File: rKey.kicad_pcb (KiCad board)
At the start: 2 copper layers, 52.8 x 71.4 mm, 39 parts, among them IC1 BDX34C, J1 Conn_01x06, Q1 BC337, Q2 BC337, Q3 BC337, Q4 BC337, Q5 BC327, Q8 BC337, U1 TL084BCN, U2 LM7810_TO220

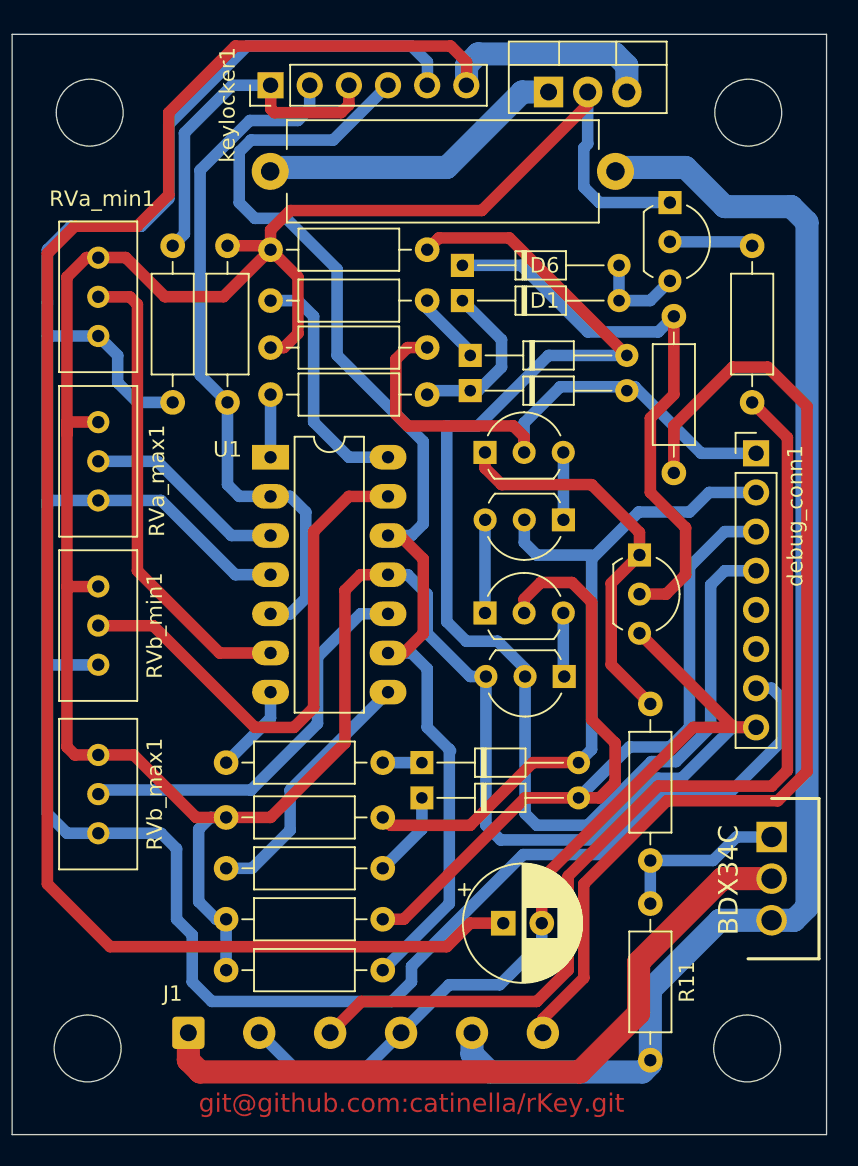
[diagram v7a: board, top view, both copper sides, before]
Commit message: Fix: unuseful (diodes) components removed
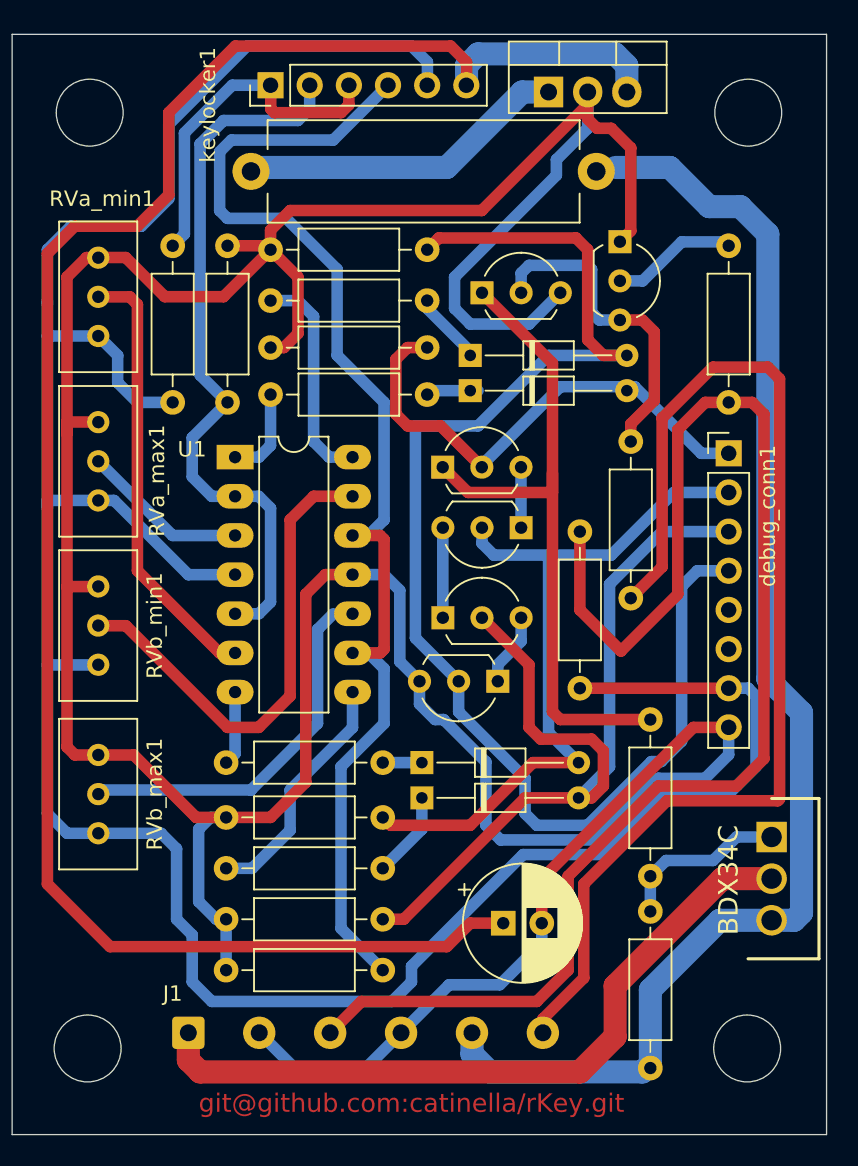
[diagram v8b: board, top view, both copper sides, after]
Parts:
- removed D1, D6: DIODE, Diode_THT:D_DO-34_SOD68_P10.16mm_Horizontal
- added R14: 100K, Resistor_THT:R_Axial_DIN0207_L6.3mm_D2.5mm_P10.16mm_Horizontal, F.Cu at (153.4, 99.1)
- moved Q8 19.8 mm to (147.1, 73.4), turned to 0 degrees
- moved R9 8.59 mm to (156.7, 83.1)
- moved Q4 4.32 mm to (148.1, 98.6)
- moved Q5 4.12 mm to (156.0, 70.1)
- moved Q1 2.91 mm to (144.5, 84.7)
- moved Q2 2.79 mm to (149.6, 88.6)
- moved Q3 2.75 mm to (144.5, 94.5)
- moved U1 2.30 mm to (131.0, 84.1)
- moved debug_conn1 1.78 mm to (163.1, 83.8)
- moved R13 1.52 mm to (163.1, 70.4)
- moved R6 1.25 mm to (132.1, 65.5)
- moved R10 1.02 mm to (158.0, 101.1)
- moved R11 0.51 mm to (158.0, 113.5)
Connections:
- Q5 pad 3: Net-(D1-Pad2) -> Net-(Q8-Pad2)
- Q8 pad 2: Net-(D6-Pad1) -> Net-(Q8-Pad2)
- R9 pad 1: Net-(D6-Pad1) -> Net-(Q8-Pad2)
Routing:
- net Net-(D6-Pad1): track 37.8 -> 0.00 mm
- net Net-(R14-Pad2): track 65.1 -> 92.8 mm
- net Net-(Q8-Pad2): track 0.00 -> 21.3 mm
- net Net-(Q1-Pad1): track 25.7 -> 44.7 mm
- net GND: track 244.1 -> 256.8 mm
- net Net-(J1-Pad6): track 66.3 -> 74.8 mm
- net Net-(R2-Pad2): track 10.9 -> 3.41 mm
- net Net-(R1-Pad1): track 172.2 -> 179.0 mm
- net Net-(D1-Pad2): track 6.12 -> 0.00 mm
- net Net-(Q3-Pad2): track 62.1 -> 57.8 mm
- net Net-(Q4-Pad2): track 86.0 -> 89.8 mm
- net Net-(Q5-Pad2): track 5.44 -> 8.21 mm
- net Net-(Q1-Pad2): track 35.6 -> 32.9 mm
- net Net-(RVa_max1-Pad2): track 13.2 -> 10.6 mm
- net Net-(RVb_min1-Pad2): track 34.4 -> 31.9 mm
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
